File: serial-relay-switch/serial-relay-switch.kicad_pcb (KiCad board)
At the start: 2 copper layers, 170.2 x 66 mm, 76 parts, among them J1 Screw_Terminal_01x01, J10 Screw_Terminal_01x01, J11 Screw_Terminal_01x01, J17 Conn_01x01, J18 Conn_01x01, J19 Screw_Terminal_01x01, J2 2501551-4, J20 Screw_Terminal_01x01, J21 Conn_01x01, J4 Screw_Terminal_01x01, J5 Screw_Terminal_01x01, J6 Screw_Terminal_01x01, J7 Screw_Terminal_01x01, J8 Screw_Terminal_01x01, J9 Screw_Terminal_01x01, K1 G2RL-1-E, K2 G2RL-1-E, K3 G2RL-1-E, K4 G2RL-1-E, K5 G2RL-1-E, K6 G2RL-1-E, K7 G2RL-1-E, K8 G2RL-1-E, U1 H11L1, U13 STM1810T, U14 74LVC1G32, U15 74LVC1G08, U16 74LVC1G04, U17 74LS163, U2 ISL8488E, U3 SZNUD3124DMT1G, U4 ISL8488E, U5 74HC594, U6 SZNUD3124DMT1G, U7 SZNUD3124DMT1G, U8 SZNUD3124DMT1G

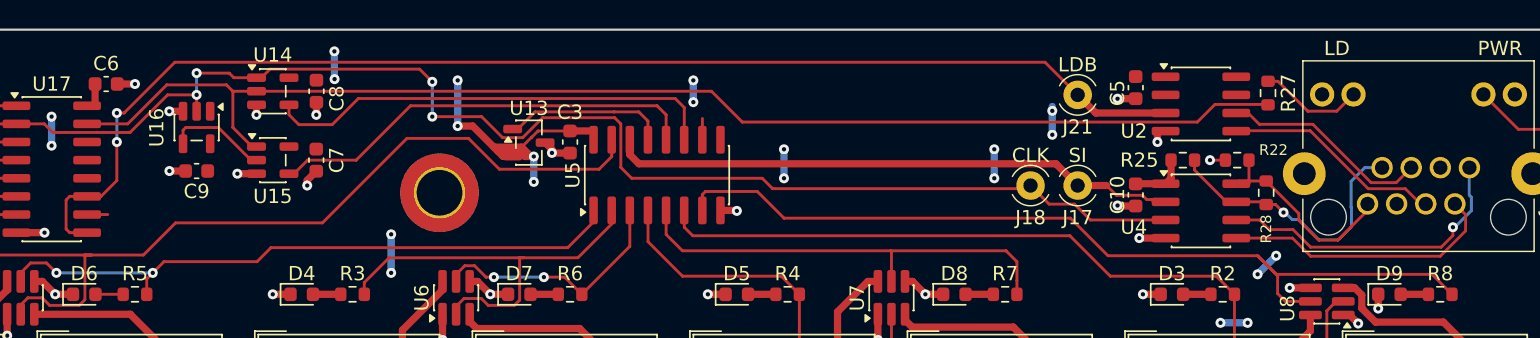
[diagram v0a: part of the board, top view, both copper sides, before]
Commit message: [rs] Correct timing in LOADB signal
Moved the LOAD signal to be from the counter's
RCO instead of the MSb of the count. This moves
the load pulse one clock cycle earlier and corrects
an off-by-one error in the receive shift register
timing, causing relay H to not be controllable
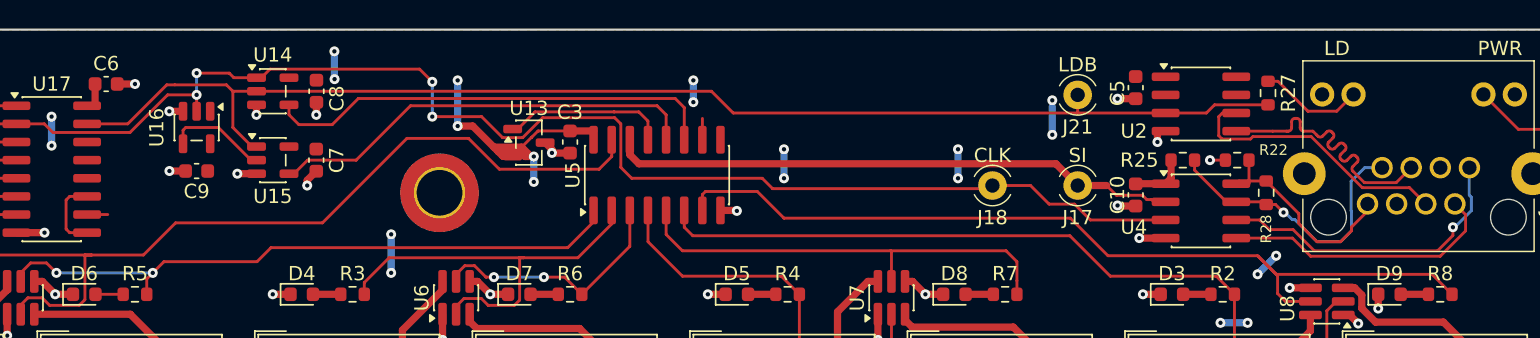
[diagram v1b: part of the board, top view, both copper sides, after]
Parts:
- moved J18 2.67 mm to (161.6, 53.5)
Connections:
- J21 pad 1: /LOADB -> /COUNT_RCO
- U17 pad 11: /LOADB -> Net-(U17-Q3)
- U17 pad 9: /LOADB -> Net-(U17-Q3)
- U2 pad 3: /LOADB -> /COUNT_RCO
- U2 pad 5: /LD_P -> /LD_N
- U2 pad 6: /LD_N -> /LD_P
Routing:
- net /LOADB: track 88.9 -> 0.00 mm, vias 2 -> 0
- net /LD_N: track 14.7 -> 20.0 mm
- net Net-(U17-Q3): track 0.00 -> 5.19 mm
- net /LD_P: track 15.4 -> 20.1 mm
- net /COUNT_RCO: track 90.2 -> 91.0 mm
